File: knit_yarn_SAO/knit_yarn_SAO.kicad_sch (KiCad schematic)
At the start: 14 parts, among them SW1 SW_SPST

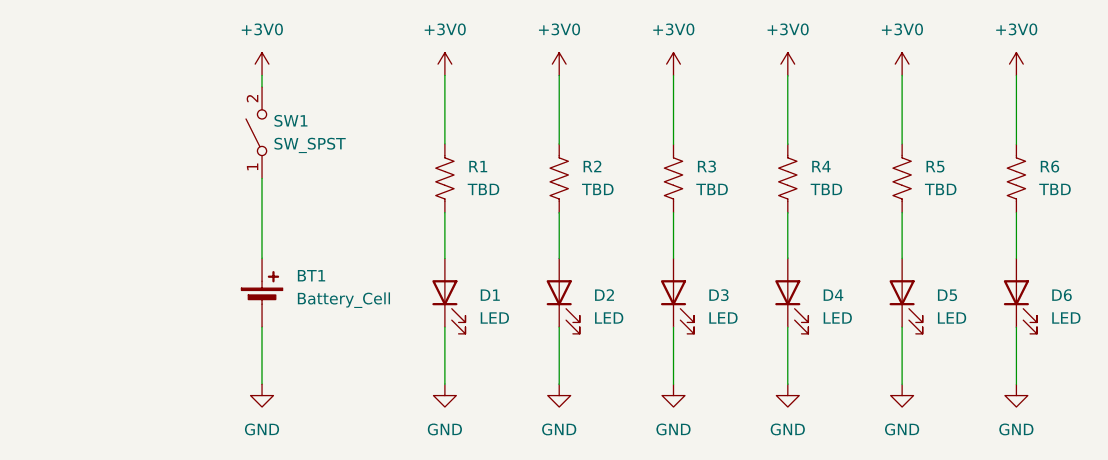
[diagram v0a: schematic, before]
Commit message: SAO connected and errors checked
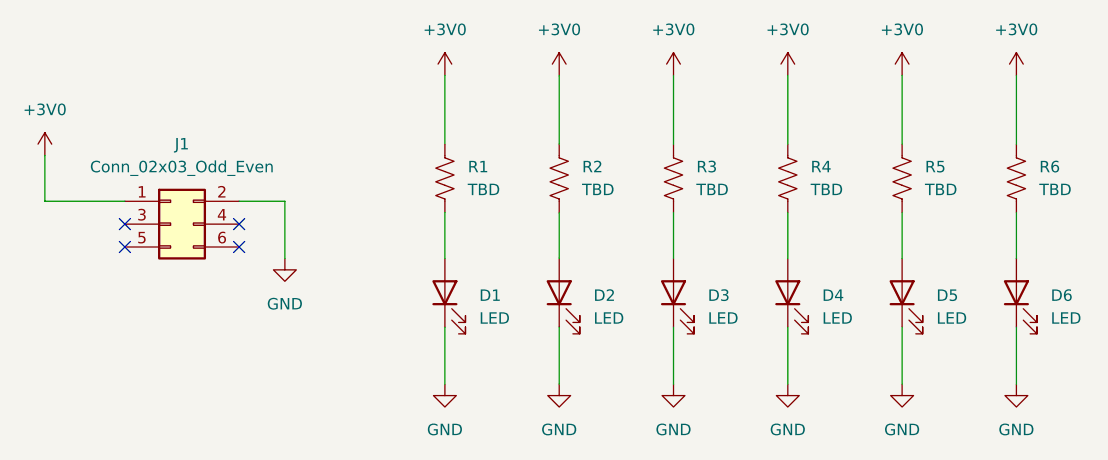
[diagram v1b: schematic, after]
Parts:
- removed BT1: Battery_Cell, Battery:BatteryHolder_Keystone_3002_1x2032, symbol Device:Battery_Cell
- removed SW1: SW_SPST, Boris_Custom:brooch_SW_20mm, symbol Switch:SW_SPST
- added J1: Conn_02x03_Odd_Even, Connector_IDC:IDC-Header_2x03_P2.54mm_Vertical_SMD, symbol Connector_Generic:Conn_02x03_Odd_Even
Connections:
- net +3V0: now also J1.1 (Pin_1)
- net GND: now also J1.2 (Pin_2)
- no-connect marks 0 -> 4
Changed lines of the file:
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@@
 		(company "Boris Nimcevic")
 	)
+	(no_connect
+		(at 101.6 93.98)
+	)
+	(no_connect
+		(at 114.3 93.98)
+	)
+	(no_connect
+		(at 114.3 91.44)
+	)
+	(no_connect
+		(at 101.6 91.44)
+	)
 	(wire
 		(pts
@@
 	(wire
 		(pts
-			(xy 116.84 102.87) (xy 116.84 109.22)
-		)
-		(stroke
-			(width 0)
-			(type default)
-		)
-	)
-	(wire
-		(pts
 			(xy 175.26 102.87) (xy 175.26 109.22)
 		)
@@
 	(wire
 		(pts
-			(xy 116.84 74.93) (xy 116.84 76.2)
+			(xy 92.71 88.9) (xy 101.6 88.9)
 		)
 		(stroke
@@
 	(wire
 		(pts
+			(xy 119.38 88.9) (xy 114.3 88.9)
+		)
+		(stroke
+			(width 0)
+			(type default)
+		)
+	)
+	(wire
+		(pts
+			(xy 92.71 83.82) (xy 92.71 88.9)
+		)
+		(stroke
+			(width 0)
+			(type default)
+		)
+	)
+	(wire
+		(pts
+			(xy 119.38 95.25) (xy 119.38 88.9)
+		)
+		(stroke
+			(width 0)
+			(type default)
+		)
+	)
+	(wire
+		(pts
 			(xy 149.86 102.87) (xy 149.86 109.22)
-		)
-		(stroke
-			(width 0)
-			(type default)
-		)
-	)
-	(wire
-		(pts
-			(xy 116.84 86.36) (xy 116.84 95.25)
 		)
 		(stroke
@@
 	(symbol
 		(lib_id "power:GND")
-		(at 116.84 109.22 0)
+		(at 119.38 95.25 0)
 		(unit 1)
 		(exclude_from_sim no)
@@
 		(fields_autoplaced yes)
 		(property "Reference" "#PWR06"
-			(at 116.84 115.57 0)
+			(at 119.38 101.6 0)
 			(effects
 				(font
@@
 		)
 		(property "Value" "GND"
-			(at 116.84 114.3 0)
+			(at 119.38 100.33 0)
 			(effects
 				(font
@@
 		)
 		(property "Footprint" ""
-			(at 116.84 109.22 0)
+			(at 119.38 95.25 0)
 			(effects
 				(font
@@
 		)
 		(property "Datasheet" ""
-			(at 116.84 109.22 0)
+			(at 119.38 95.25 0)
 			(effects
 				(font
@@
 		)
 		(property "Description" "Power symbol creates a global label with name \"GND\" , ground"
-			(at 116.84 109.22 0)
+			(at 119.38 95.25 0)
 			(effects
 				(font
@@
 	(symbol
 		(lib_id "power:+3V0")
-		(at 116.84 74.93 0)
+		(at 92.71 83.82 0)
 		(unit 1)
 		(exclude_from_sim no)
@@
 		(fields_autoplaced yes)
 		(property "Reference" "#PWR01"
-			(at 116.84 78.74 0)
+			(at 92.71 87.63 0)
 			(effects
 				(font
@@
 		)
 		(property "Value" "+3V0"
-			(at 116.84 69.85 0)
+			(at 92.71 78.74 0)
 			(effects
 				(font
@@
 		)
 		(property "Footprint" ""
-			(at 116.84 74.93 0)
+			(at 92.71 83.82 0)
 			(effects
 				(font
@@
 		)
 		(property "Datasheet" ""
-			(at 116.84 74.93 0)
+			(at 92.71 83.82 0)
 			(effects
 				(font
@@
 		)
 		(property "Description" "Power symbol creates a global label with name \"+3V0\""
-			(at 116.84 74.93 0)
+			(at 92.71 83.82 0)
 			(effects
 				(font
@@
 	)
 	(symbol
+		(lib_id "Connector_Generic:Conn_02x03_Odd_Even")
+		(at 106.68 91.44 0)
+		(unit 1)
+		(exclude_from_sim no)
+		(in_bom yes)
+		(on_board yes)
+		(dnp no)
+		(fields_autoplaced yes)
+		(property "Reference" "J1"
+			(at 107.95 82.55 0)
+			(effects
+				(font
+					(size 1.27 1.27)
+				)
+			)
+		)
+		(property "Value" "Conn_02x03_Odd_Even"
+			(at 107.95 85.09 0)
+			(effects
+				(font
+					(size 1.27 1.27)
+				)
+			)
+		)
+		(property "Footprint" "Connector_IDC:IDC-Header_2x03_P2.54mm_Vertical_SMD"
+			(at 106.68 91.44 0)
+			(effects
+				(font
+					(size 1.27 1.27)
+				)
+				(hide yes)
+			)
+		)
+		(property "Datasheet" "~"
+			(at 106.68 91.44 0)
+			(effects
+				(font
+					(size 1.27 1.27)
+				)
+				(hide yes)
+			)
+		)
+		(property "Description" "Generic connector, double row, 02x03, odd/even pin numbering scheme (row 1 odd numbers, row 2 even numbers), script generated (kicad-library-utils/schlib/autogen/connector/)"
+			(at 106.68 91.44 0)
+			(effects
+				(font
+					(size 1.27 1.27)
+				)
+				(hide yes)
+			)
+		)
+		(pin "1"
+		)
+		(pin "3"
+		)
+		(pin "5"
+		)
+		(pin "2"
+		)
+		(pin "4"
+		)
+		(pin "6"
+		)
+		(instances
+			(project ""
+				(path "/3c87448c-fe54-4cb9-8063-41ec64699176"
+					(reference "J1")
+					(unit 1)
+				)
+			)
+		)
+	)
+	(symbol
 		(lib_id "power:GND")
 		(at 200.66 109.22 0)
@@
 	)
 	(symbol
-		(lib_id "Device:Battery_Cell")
-		(at 116.84 100.33 0)
-		(unit 1)
-		(exclude_from_sim no)
-		(in_bom yes)
-		(on_board yes)
-		(dnp no)
-		(fields_autoplaced yes)
-		(property "Reference" "BT1"
-			(at 120.65 97.2184 0)
-			(effects
-				(font
-					(size 1.27 1.27)
-				)
-				(justify left)
-			)
-		)
-		(property "Value" "Battery_Cell"
-			(at 120.65 99.7584 0)
-			(effects
-				(font
-					(size 1.27 1.27)
-				)
-				(justify left)
-			)
-		)
-		(property "Footprint" "Battery:BatteryHolder_Keystone_3002_1x2032"
-			(at 116.84 98.806 90)
-			(effects
-				(font
-					(size 1.27 1.27)
-				)
-				(hide yes)
-			)
-		)
-		(property "Datasheet" "~"
-			(at 116.84 98.806 90)
-			(effects
-				(font
-					(size 1.27 1.27)
-				)
-				(hide yes)
-			)
-		)
-		(property "Description" "Single-cell battery"
-			(at 116.84 100.33 0)
-			(effects
-				(font
-					(size 1.27 1.27)
-				)
-				(hide yes)
-			)
-		)
-		(pin "1"
-		)
-		(pin "2"
-		)
-		(instances
-			(project ""
-				(path "/3c87448c-fe54-4cb9-8063-41ec64699176"
-					(reference "BT1")
-					(unit 1)
-				)
-			)
-		)
-	)
-	(symbol
 		(lib_id "power:+3V0")
 		(at 175.26 74.93 0)
@@
 					(unit 1)
 				)
-			)
-		)
-	)
-	(symbol
-		(lib_id "Switch:SW_SPST")
-		(at 116.84 81.28 90)
-		(unit 1)
-		(exclude_from_sim no)
-		(in_bom yes)
-		(on_board yes)
-		(dnp no)
-		(fields_autoplaced yes)
-		(property "Reference" "SW1"
-			(at 118.11 80.0099 90)
-			(effects
-				(font
-					(size 1.27 1.27)
-				)
-				(justify right)
-			)
-		)
-		(property "Value" "SW_SPST"
-			(at 118.11 82.5499 90)
-			(effects
-				(font
-					(size 1.27 1.27)
-				)
-				(justify right)
-			)
-		)
-		(property "Footprint" "Boris_Custom:brooch_SW_20mm"
-			(at 116.84 81.28 0)
-			(effects
-				(font
-					(size 1.27 1.27)
-				)
-				(hide yes)
-			)
-		)
-		(property "Datasheet" "~"
-			(at 116.84 81.28 0)
-			(effects
-				(font
-					(size 1.27 1.27)
-				)
-				(hide yes)
-			)
-		)
-		(property "Description" "Single Pole Single Throw (SPST) switch"
-			(at 116.84 81.28 0)
-			(effects
-				(font
-					(size 1.27 1.27)
-				)
-				(hide yes)
-			)
-		)
-		(pin "2"
-		)
-		(pin "1"
-		)
-		(instances
-			(project ""
-				(path "/3c87448c-fe54-4cb9-8063-41ec64699176"
-					(reference "SW1")
-					(unit 1)
-				)
